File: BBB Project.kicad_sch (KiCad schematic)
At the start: 5 parts, among them J1 Conn_02x04_Odd_Even, J2 Conn_01x02_Female, SW1 SW_Push, U1 MAX6816

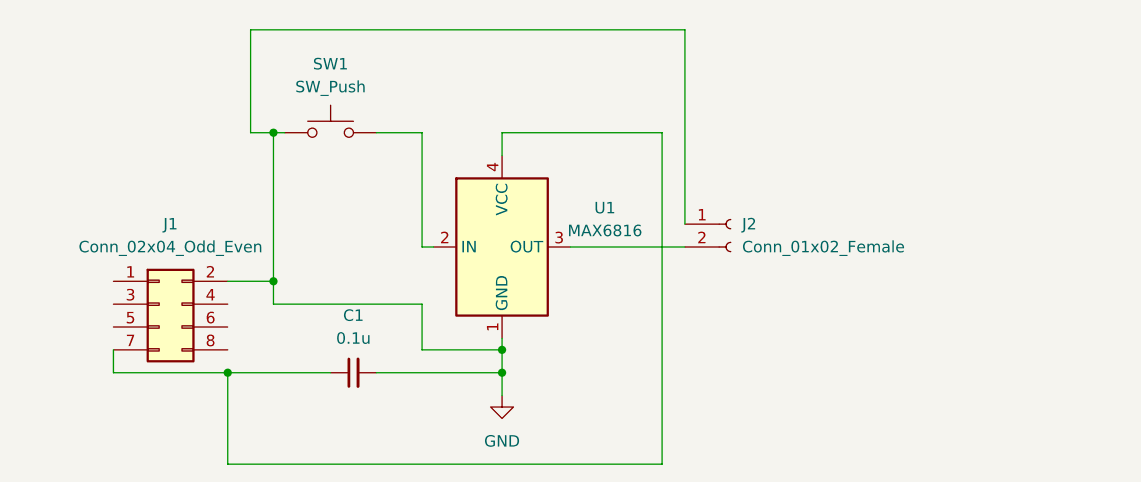
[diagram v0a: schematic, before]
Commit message: Fixed voltage and verified board
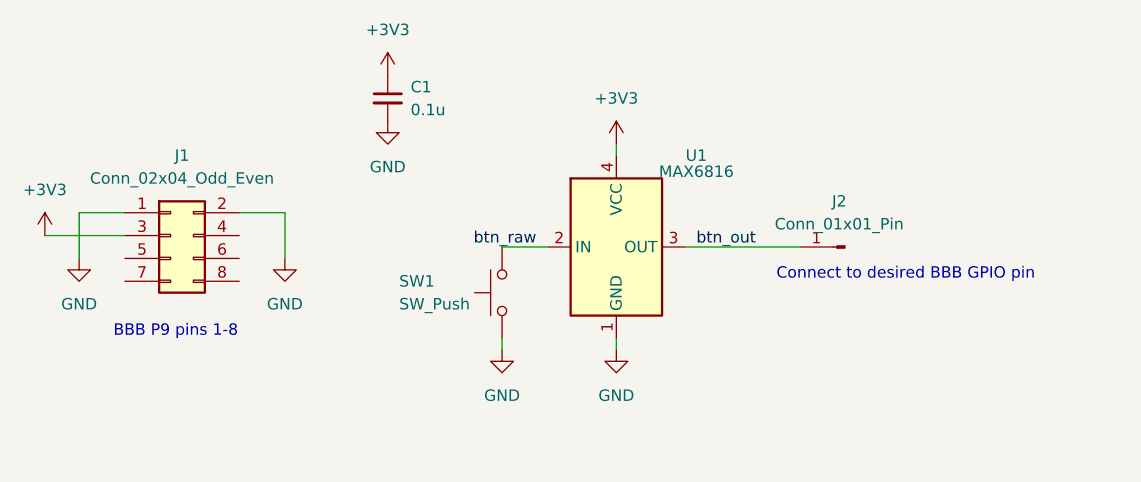
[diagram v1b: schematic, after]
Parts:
- removed J2: Conn_01x02_Female, Connector_PinHeader_2.54mm:PinHeader_1x02_P2.54mm_Vertical, symbol Connector:Conn_01x02_Female
- added J2: Conn_01x01_Pin, Connector_Wire:SolderWire-0.25sqmm_1x01_D0.65mm_OD2mm_Relief2x, symbol Connector:Conn_01x01_Pin
- C1: footprint Capacitor_THT:C_Disc_D5.0mm_W2.5mm_P5.00mm -> Capacitor_SMD:C_0805_2012Metric
- SW1: footprint Button_Switch_THT:SW_PUSH_6mm -> Button_Switch_SMD:SW_Push_1P1T_NO_6x6mm_H9.5mm
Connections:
- net GND: now also J1.1 (Pin_1)
- net btn_raw: now reaches SW1.2, U1.2 (IN)
- net btn_out: now reaches U1.3 (OUT)
- net btn_out: now also J2.1 (Pin_1)
- net +3V3: now reaches C1.1, U1.4 (VCC)
- net +3V3: now also J1.3 (Pin_3); no longer J1.7 (Pin_7)
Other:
- note added: "BBB P9 pins 1-8"
- note added: "Connect to desired BBB GPIO pin"
- moved on the sheet: C1, J1, SW1, U1
